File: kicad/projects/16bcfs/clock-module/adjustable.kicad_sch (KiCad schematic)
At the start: 5 parts, among them U8 NE555D

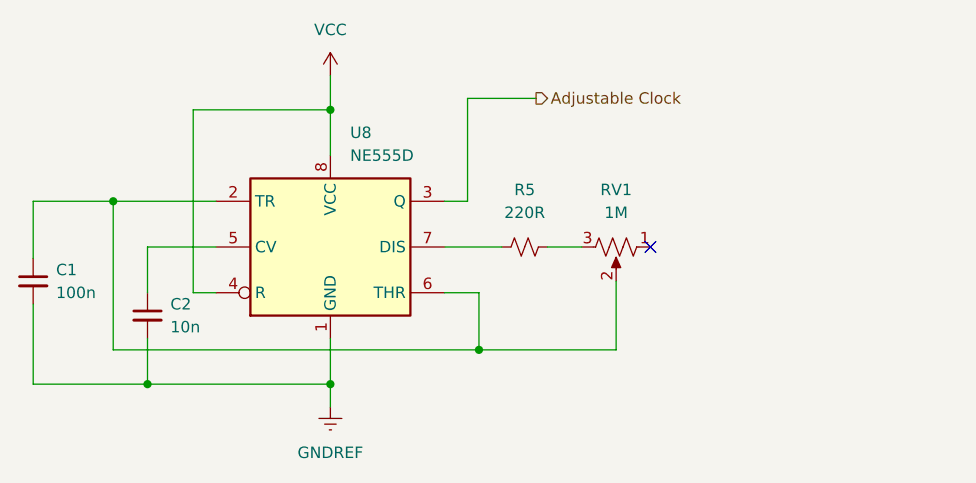
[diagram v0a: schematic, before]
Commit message: Clean up the Reset and Clock Modules
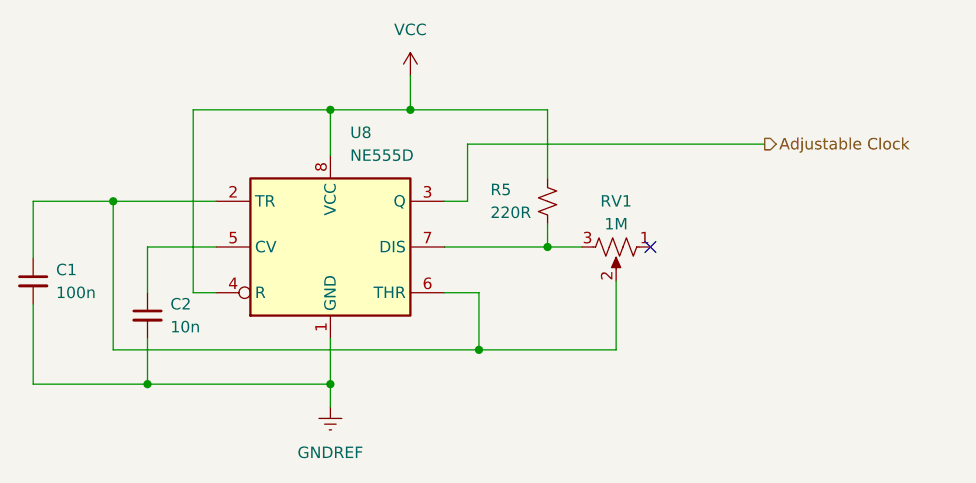
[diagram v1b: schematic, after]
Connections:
- net VCC: now also R5.2
- net at R5.1, U8.7 (DIS): now also RV1.3
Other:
- moved on the sheet: R5
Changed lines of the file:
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@@
   (junction (at 105.41 90.17) (diameter 0) (color 0 0 0 0)
   )
+  (junction (at 153.67 95.25) (diameter 0) (color 0 0 0 0)
+  )
   (junction (at 146.05 106.68) (diameter 0) (color 0 0 0 0)
   )
   (junction (at 109.22 110.49) (diameter 0) (color 0 0 0 0)
   )
+  (junction (at 138.43 80.01) (diameter 0) (color 0 0 0 0)
+  )
   (no_connect (at 165.1 95.25))
+  (wire (pts (xy 153.67 95.25) (xy 157.48 95.25))
+    (stroke (width 0) (type default))
+  )
   (wire (pts (xy 116.84 90.17) (xy 105.41 90.17))
     (stroke (width 0) (type default))
   )
-  (wire (pts (xy 157.48 95.25) (xy 153.67 95.25))
-    (stroke (width 0) (type default))
-  )
   (wire (pts (xy 105.41 106.68) (xy 146.05 106.68))
     (stroke (width 0) (type default))
   )
+  (wire (pts (xy 153.67 80.01) (xy 138.43 80.01))
+    (stroke (width 0) (type default))
+  )
   (wire (pts (xy 105.41 90.17) (xy 96.52 90.17))
     (stroke (width 0) (type default))
@@
     (stroke (width 0) (type default))
   )
-  (wire (pts (xy 144.78 78.74) (xy 152.4 78.74))
+  (wire (pts (xy 144.78 83.82) (xy 177.8 83.82))
     (stroke (width 0) (type default))
   )
@@
     (stroke (width 0) (type default))
   )
+  (wire (pts (xy 138.43 80.01) (xy 129.54 80.01))
+    (stroke (width 0) (type default))
+  )
   (wire (pts (xy 129.54 80.01) (xy 129.54 85.09))
     (stroke (width 0) (type default))
@@
     (stroke (width 0) (type default))
   )
-  (wire (pts (xy 129.54 76.2) (xy 129.54 80.01))
+  (wire (pts (xy 138.43 76.2) (xy 138.43 80.01))
     (stroke (width 0) (type default))
   )
@@
     (stroke (width 0) (type default))
   )
-  (wire (pts (xy 144.78 78.74) (xy 144.78 90.17))
+  (wire (pts (xy 142.24 95.25) (xy 153.67 95.25))
+    (stroke (width 0) (type default))
+  )
+  (wire (pts (xy 144.78 83.82) (xy 144.78 90.17))
     (stroke (width 0) (type default))
   )
@@
     (stroke (width 0) (type default))
   )
+  (wire (pts (xy 153.67 92.71) (xy 153.67 95.25))
+    (stroke (width 0) (type default))
+  )
   (wire (pts (xy 116.84 100.33) (xy 114.3 100.33))
     (stroke (width 0) (type default))
@@
     (stroke (width 0) (type default))
   )
+  (wire (pts (xy 153.67 87.63) (xy 153.67 80.01))
+    (stroke (width 0) (type default))
+  )
   (wire (pts (xy 161.29 99.06) (xy 161.29 106.68))
     (stroke (width 0) (type default))
   )
-  (wire (pts (xy 148.59 95.25) (xy 142.24 95.25))
-    (stroke (width 0) (type default))
-  )
-  (hierarchical_label "Adjustable Clock" (shape output) (at 152.4 78.74 0) (fields_autoplaced)
+  (hierarchical_label "Adjustable Clock" (shape output) (at 177.8 83.82 0) (fields_autoplaced)
     (effects (font (size 1.27 1.27)) (justify left))
   )
-  (symbol (lib_id "Device:R_Small_US") (at 151.13 95.25 90) (unit 1)
-    (in_bom yes) (on_board yes) (dnp no) (fields_autoplaced)
-    (property "Reference" "R5" (at 151.13 88.9 90)
-      (effects (font (size 1.27 1.27)))
-    )
-    (property "Value" "220R" (at 151.13 91.44 90)
-      (effects (font (size 1.27 1.27)))
-    )
-    (property "Footprint" "" (at 151.13 95.25 0)
-      (effects (font (size 1.27 1.27)) hide)
-    )
-    (property "Datasheet" "~" (at 151.13 95.25 0)
+  (symbol (lib_id "Device:R_Small_US") (at 153.67 90.17 180) (unit 1)
+    (in_bom yes) (on_board yes) (dnp no)
+    (property "Reference" "R5" (at 147.32 88.9 0)
+      (effects (font (size 1.27 1.27)) (justify right))
+    )
+    (property "Value" "220R" (at 147.32 91.44 0)
+      (effects (font (size 1.27 1.27)) (justify right))
+    )
+    (property "Footprint" "" (at 153.67 90.17 0)
+      (effects (font (size 1.27 1.27)) hide)
+    )
+    (property "Datasheet" "~" (at 153.67 90.17 0)
       (effects (font (size 1.27 1.27)) hide)
     )
@@
     )
   )
-  (symbol (lib_id "power:VCC") (at 129.54 76.2 0) (unit 1)
-    (in_bom yes) (on_board yes) (dnp no) (fields_autoplaced)
-    (property "Reference" "#PWR07" (at 129.54 80.01 0)
-      (effects (font (size 1.27 1.27)) hide)
-    )
-    (property "Value" "VCC" (at 129.54 71.12 0)
-      (effects (font (size 1.27 1.27)))
-    )
-    (property "Footprint" "" (at 129.54 76.2 0)
-      (effects (font (size 1.27 1.27)) hide)
-    )
-    (property "Datasheet" "" (at 129.54 76.2 0)
+  (symbol (lib_id "power:VCC") (at 138.43 76.2 0) (unit 1)
+    (in_bom yes) (on_board yes) (dnp no) (fields_autoplaced)
+    (property "Reference" "#PWR07" (at 138.43 80.01 0)
+      (effects (font (size 1.27 1.27)) hide)
+    )
+    (property "Value" "VCC" (at 138.43 71.12 0)
+      (effects (font (size 1.27 1.27)))
+    )
+    (property "Footprint" "" (at 138.43 76.2 0)
+      (effects (font (size 1.27 1.27)) hide)
+    )
+    (property "Datasheet" "" (at 138.43 76.2 0)
       (effects (font (size 1.27 1.27)) hide)
     )
@@
   )
   (symbol (lib_id "Device:R_Potentiometer_US") (at 161.29 95.25 270) (unit 1)
-    (in_bom yes) (on_board yes) (dnp no) (fields_autoplaced)
-    (property "Reference" "RV1" (at 161.29 88.9 90)
-      (effects (font (size 1.27 1.27)))
-    )
-    (property "Value" "1M" (at 161.29 91.44 90)
-      (effects (font (size 1.27 1.27)))
-    )
+    (in_bom yes) (on_board yes) (dnp no)
+    (property "Reference" "RV1" (at 161.29 90.17 90)
+      (effects (font (size 1.27 1.27)))
+    )
+    (property "Value" "1M" (at 161.29 92.71 90)
+      (effects (font (size 1.27 1.27)))
+    )
